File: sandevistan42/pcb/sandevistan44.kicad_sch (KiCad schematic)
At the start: 98 parts, among them J1 TRRS, J2 TRRS, SW1 SW_PUSH, SW10 SW_PUSH, SW11 SW_PUSH, SW12 SW_PUSH, SW13 SW_PUSH, SW14 SW_PUSH, SW15 SW_PUSH, SW16 SW_PUSH, SW17 SW_PUSH, SW18 SW_PUSH, SW19 SW_PUSH, SW2 SW_PUSH, SW20 SW_PUSH, SW21 SW_PUSH, SW22 SW_PUSH, SW23 SW_PUSH, SW24 SW_PUSH, SW25 SW_PUSH, SW26 SW_PUSH, SW27 SW_PUSH, SW28 SW_PUSH, SW29 SW_PUSH, SW3 SW_PUSH, SW30 SW_PUSH, SW31 SW_PUSH, SW32 SW_PUSH, SW33 SW_PUSH, SW34 SW_PUSH, SW35 SW_PUSH, SW36 SW_PUSH, SW37 SW_PUSH, SW38 SW_PUSH, SW39 SW_PUSH, SW4 SW_PUSH, SW40 SW_PUSH, SW41 SW_PUSH, SW42 SW_PUSH, SW43 SW_PUSH, SW44 SW_PUSH, SW5 SW_PUSH, SW6 SW_PUSH, SW7 SW_PUSH, SW8 SW_PUSH, SW9 SW_PUSH, U1 ProMicro, U2 ProMicro

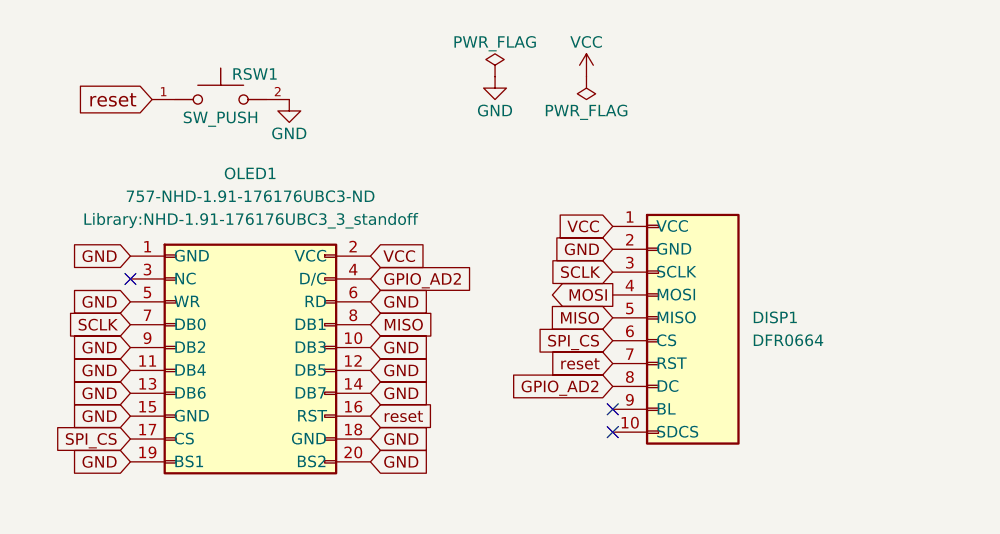
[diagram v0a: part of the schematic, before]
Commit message: Split pcbs into separate files and add plates
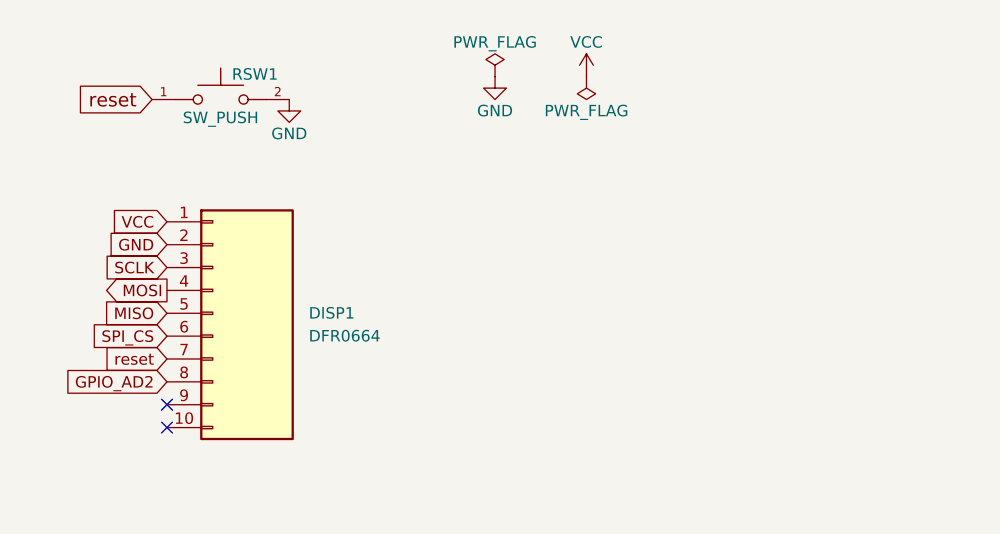
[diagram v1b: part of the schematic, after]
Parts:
- removed OLED1: 757-NHD-1.91-176176UBC3-ND, Library:NHD-1.91-176176UBC3_3_standoff, symbol sandevistan42:757-NHD-1.91-176176UBC3-ND
- DISP1: symbol sandevistan42:DFR0664 -> sandevistan44:DFR0664
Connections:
- no-connect marks 22 -> 21
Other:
- company: foostan -> islathehut
- title: Corne Cherry -> Sandevistan44
